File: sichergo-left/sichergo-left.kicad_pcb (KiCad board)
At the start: 2 copper layers, 123.4 x 96.1 mm, 117 parts, among them J1 Conn_01x04_Pin, Q1 2N7002, SW1 SW_Push, SW10 SW_Push, SW11 SW_Push, SW12 SW_Push, SW13 SW_Push, SW14 SW_Push, SW15 SW_Push, SW16 SW_Push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

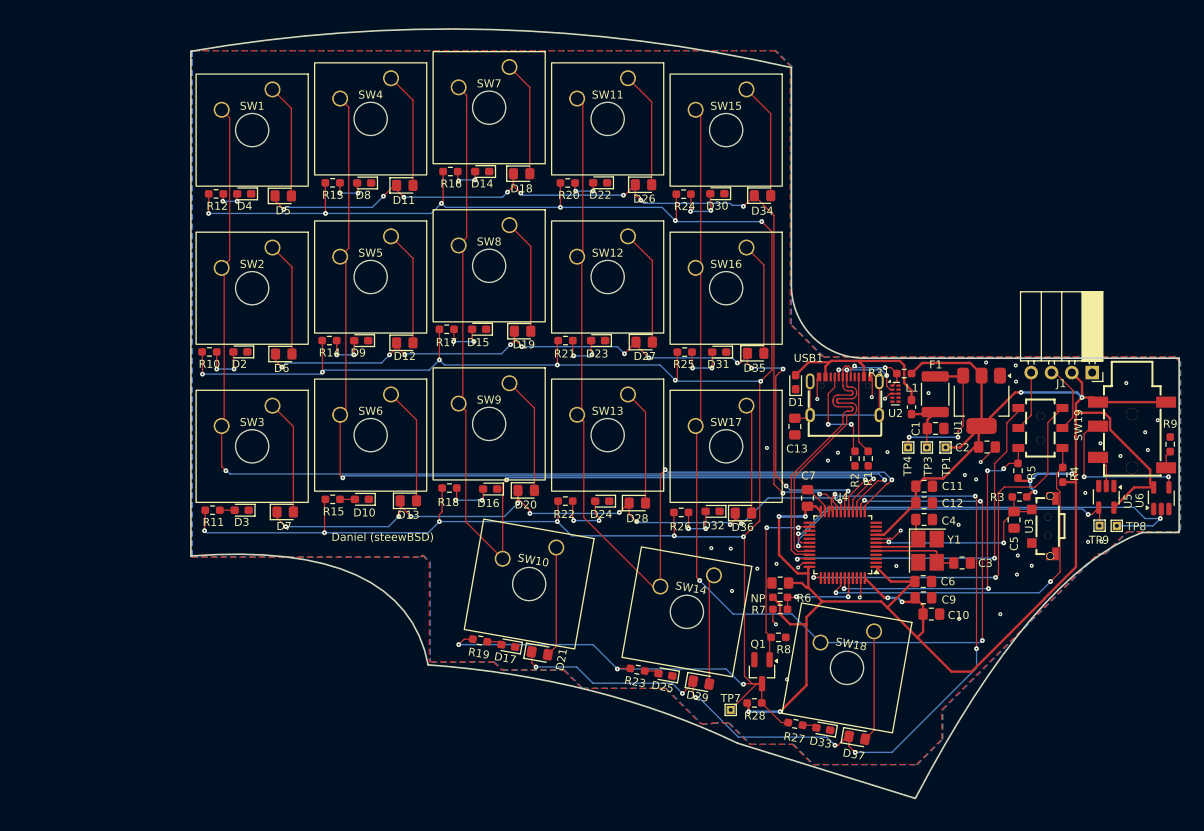
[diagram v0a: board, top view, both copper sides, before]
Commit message: Fix keyboard layout size
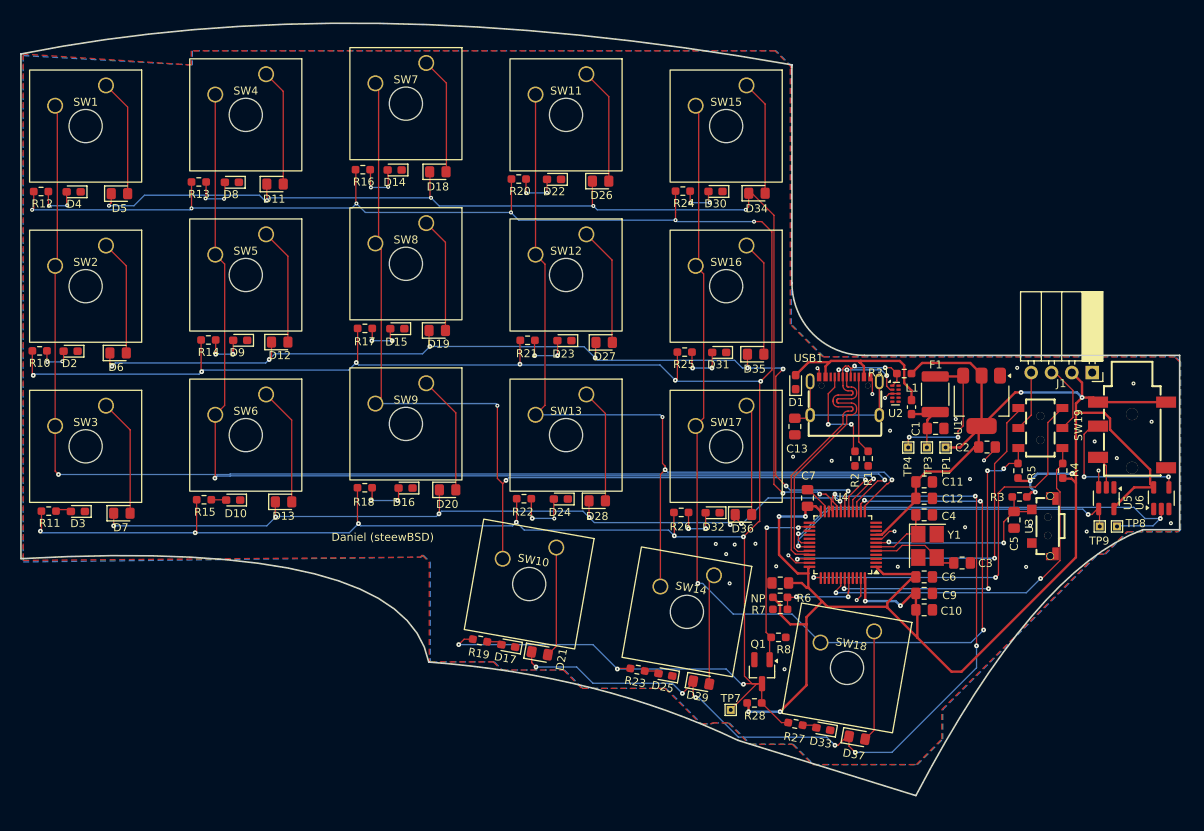
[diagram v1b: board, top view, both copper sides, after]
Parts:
- removed R9: 100 ohm, Resistor_SMD:R_0603_1608Metric_Pad0.98x0.95mm_HandSolder
- moved R12 21.9 mm to (91.3, 84.1)
- moved D4 21.3 mm to (95.4, 84.2)
- moved R10 21.2 mm to (91.2, 104.0)
- moved D2 21.2 mm to (95.0, 104.1)
- moved SW1 20.8 mm to (96.9, 76.0)
- moved SW2 20.8 mm to (96.9, 96.0)
- moved SW3 20.8 mm to (96.9, 116.0)
- moved D6 20.7 mm to (101.0, 104.3)
- moved D3 20.5 mm to (95.9, 124.1)
- moved R11 20.5 mm to (92.3, 124.0)
- moved D5 20.5 mm to (101.1, 84.4)
- moved D7 20.4 mm to (101.4, 124.3)
- moved R13 16.7 mm to (111.0, 82.9)
- moved D8 16.5 mm to (115.2, 83.0)
- moved D11 16.2 mm to (120.6, 83.2)
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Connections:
- Audio1 pad 1: Net-(Audio1-Pad1) -> GND
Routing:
- net /MatrixL/LED_DRIVE: track 377.5 -> 444.2 mm
- net /KB_ROW_0: track 115.4 -> 141.5 mm, vias 10 -> 7
- net /KB_ROW_1: track 99.4 -> 122.6 mm, vias 12 -> 8
- net /KB_COL_0: track 134.1 -> 155.1 mm
- net /KB_ROW_2: track 85.3 -> 105.4 mm, vias 10 -> 7
- net /KB_COL_1: track 120.7 -> 136.6 mm
- net /KB_COL_2: track 120.9 -> 125.1 mm, vias 2 -> 3
- net /KB_COL_4: track 128.5 -> 131.4 mm
- net +3V3: track 241.8 -> 244.5 mm
- net Net-(D14-A): track 4.37 -> 6.92 mm
- net Net-(D4-A): track 3.64 -> 5.90 mm
- net Net-(Audio1-Pad1): track 2.23 -> 0.00 mm
- net Net-(D22-A): track 4.25 -> 6.18 mm
- net Net-(U4-PD1): track 7.80 -> 9.64 mm
- net Net-(D2-A): track 6.47 -> 4.64 mm
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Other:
- board size 123.4 x 96.1 mm -> 144.7 x 96.5 mm

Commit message: Fix copper pour shape
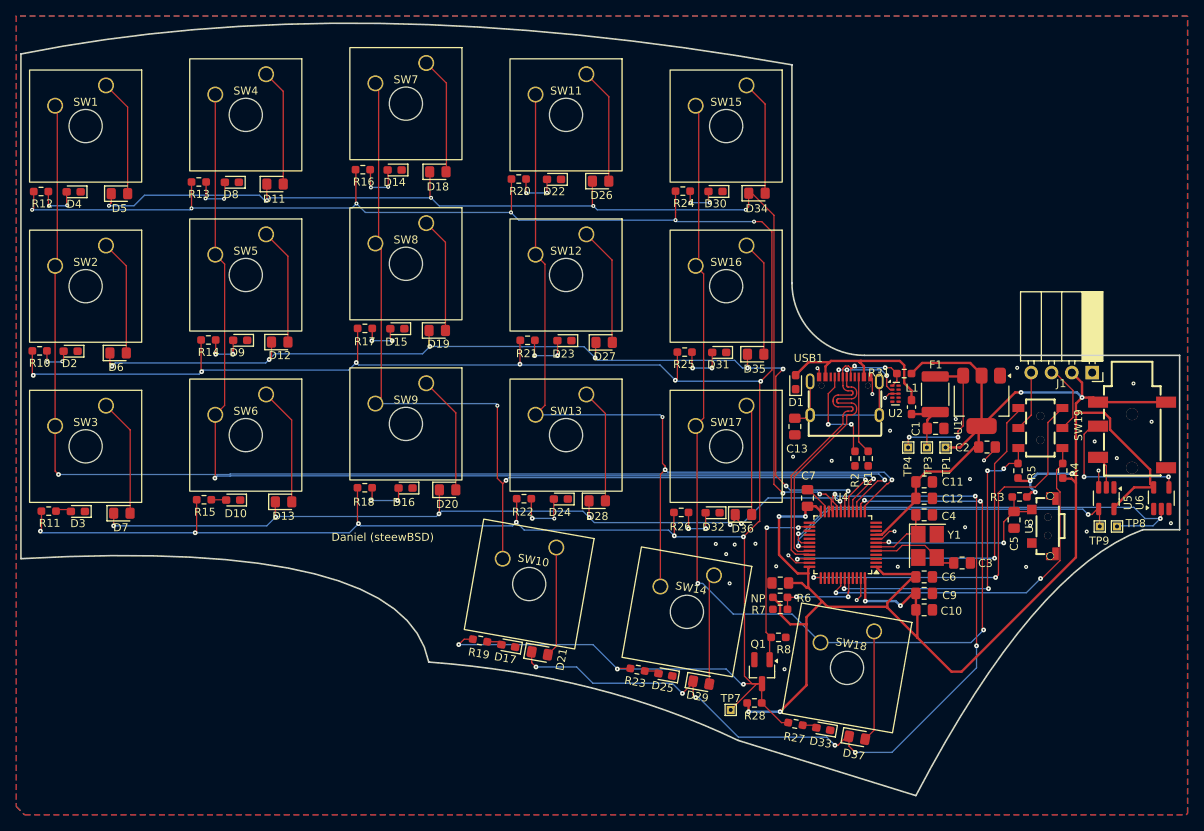
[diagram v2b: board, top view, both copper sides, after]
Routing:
- net +3V3: track 244.5 -> 242.7 mm
- net Net-(U4-PD1): track 9.64 -> 8.69 mm
- net /KB_ROW_2: track 105.4 -> 104.6 mm

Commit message: fix left side USB C
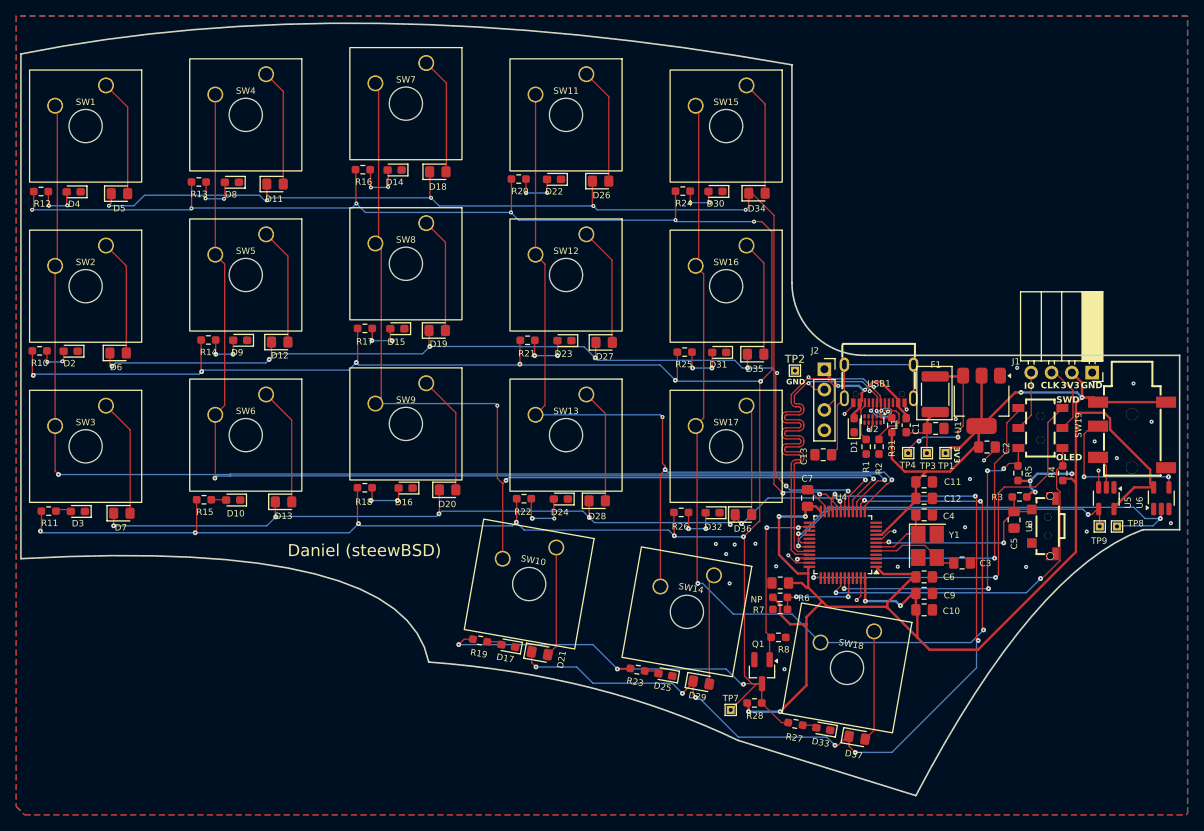
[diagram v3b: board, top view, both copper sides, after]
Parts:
- added J2: Conn_01x04_Pin, Connector_PinSocket_2.54mm:PinSocket_1x04_P2.54mm_Vertical, F.Cu at (189.2, 106.3)
- added TP2: TestPoint, TestPoint:TestPoint_THTPad_1.0x1.0mm_Drill0.5mm, F.Cu at (185.5, 106.5)
- moved D1 9.07 mm to (192.9, 113.3)
- moved R31 6.64 mm to (197.6, 113.3), turned to 90 degrees
- moved C13 5.00 mm to (189.0, 117.0), turned to 180 degrees
- moved USB1 4.54 mm to (196.0, 108.1), turned to 180 degrees
- moved U2 4.31 mm to (195.2, 112.6), turned to -90 degrees
- moved R2 3.35 mm to (196.0, 116.0)
- moved L1 2.36 mm to (199.4, 113.3)
- moved R1 1.50 mm to (194.4, 116.0)
- moved TP1 0.70 mm to (204.3, 116.8)
- moved TP3 0.70 mm to (202.0, 116.8)
- moved TP4 0.70 mm to (199.7, 116.8)
- moved R4 0.30 mm to (218.9, 119.3)
- moved R5 0.30 mm to (213.4, 119.3)
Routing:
- net /D+: track 44.0 -> 65.8 mm, vias 2 -> 4
- net /D-: track 42.3 -> 55.5 mm, vias 3 -> 4
- net Net-(C13-Pad1): track 18.6 -> 24.8 mm
- net Net-(USB1-CC1): track 12.4 -> 6.91 mm, vias 2 -> 0
- net /VBUS: track 23.8 -> 19.1 mm, vias 0 -> 2
- net Net-(USB1-CC2): track 9.77 -> 5.06 mm
- net +3V3: track 242.7 -> 238.5 mm
- net /KB_ROW_1: track 122.6 -> 121.2 mm
- net Net-(C1-Pad1): track 7.49 -> 8.35 mm
- net GND: track 21.5 -> 21.0 mm, vias 31 -> 28
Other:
- board text added: "3V3"
- board text added: "CLK"
- board text added: "GND"
- board text added: "IO"
- board text added: "OLED"
- board text added: "SWD"
